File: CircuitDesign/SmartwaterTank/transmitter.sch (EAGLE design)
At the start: 9 parts, among them IC1 MEGA8-P

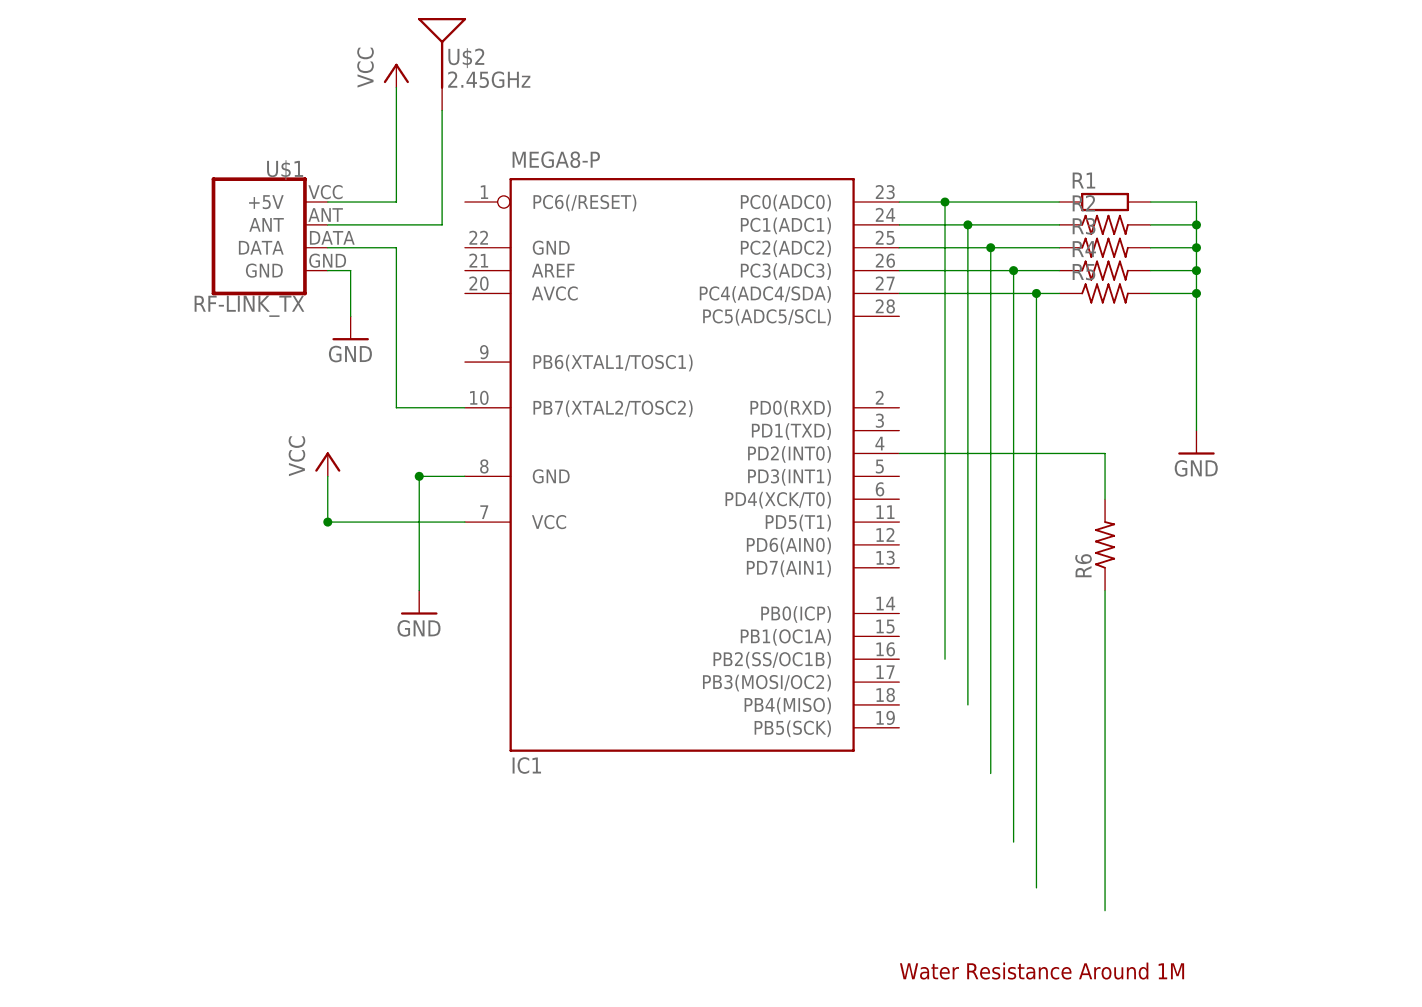
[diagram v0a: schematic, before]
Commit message: implement distance sensor in water level detection
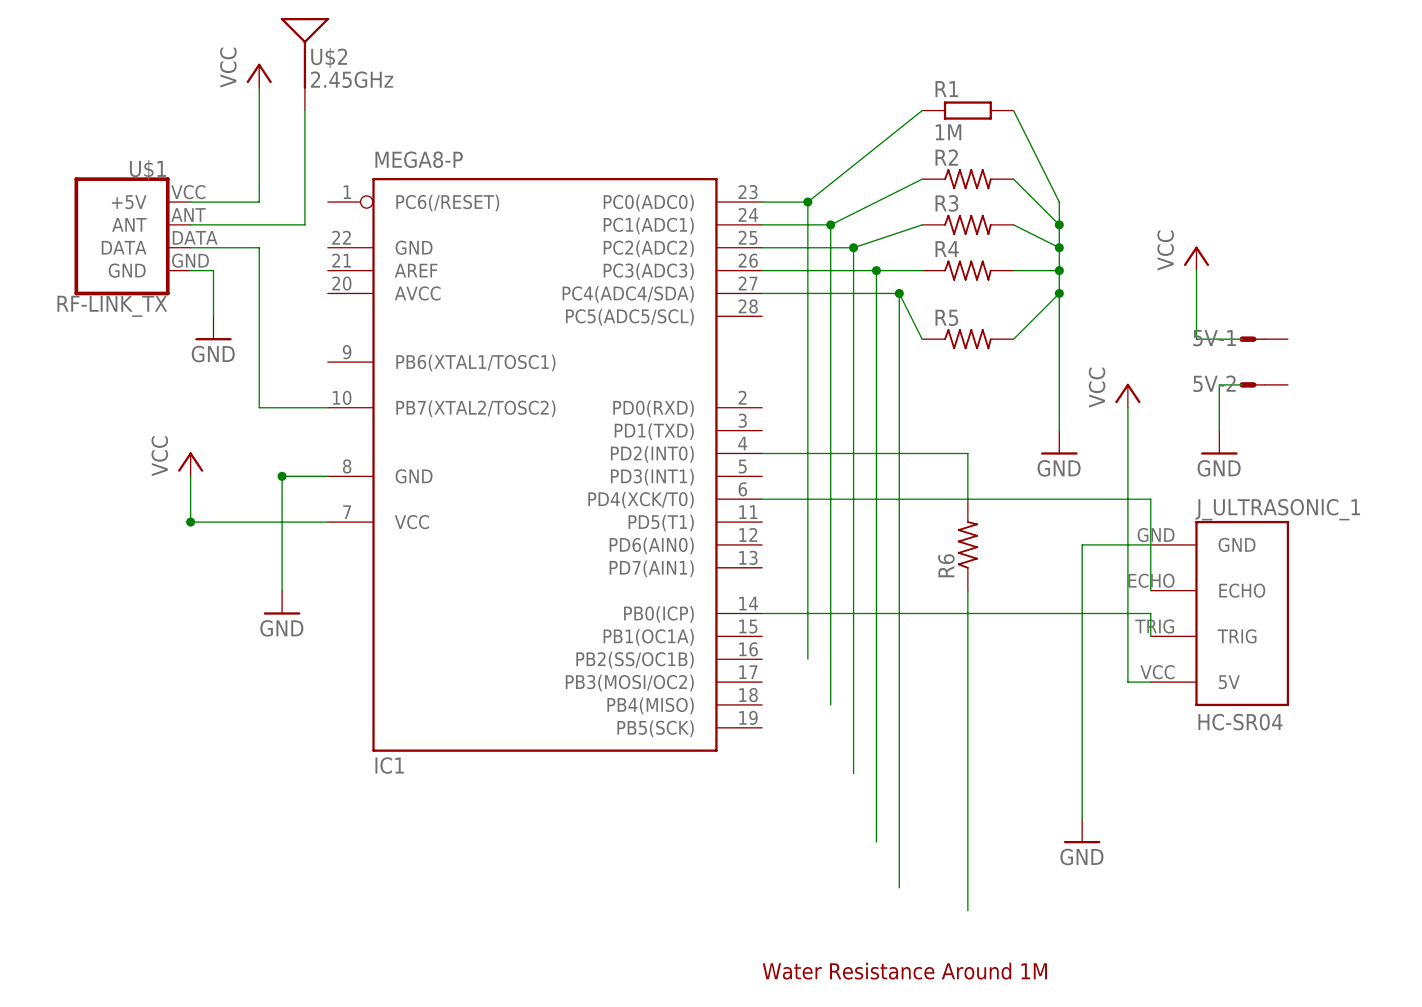
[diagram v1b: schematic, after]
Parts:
- added 5V: (no value), con-amp-mt:S02P
- added J_ULTRASONIC_1: HC-SR04, Ultrasonic Sensor HC-SR04:HC-SR04
- R1: value (none) -> 1M
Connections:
- new net N$10: IC1.PD4(XCK/T0), J_ULTRASONIC_1.ECHO
- new net N$11: IC1.PB0(ICP), J_ULTRASONIC_1.TRIG
- net GND: now also J_ULTRASONIC_1.GND
- net VCC: now also J_ULTRASONIC_1.5V
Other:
- moved on the sheet: IC1, R1, R2, R3, R4, R5, R6, U$1, U$2
